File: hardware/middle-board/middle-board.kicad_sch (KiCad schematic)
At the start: 25 parts, among them J1 Conn_01x10_Socket, J2 Conn_01x15_Socket, J3 Conn_01x10_Pin, J4 Conn_01x09_Socket, J5 Conn_01x09_Socket, J6 Conn_01x12_Pin, U1 TL084, U2 TL074, U3 TL072, U4 NE5517

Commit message: wip - first pass done
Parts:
- C10, C3, C4, C5, C6, C7, C8, C9: footprint Capacitor_THT:C_Rect_L4.6mm_W3.0mm_P2.50mm_MKS02_FKP02 -> Eurorack Common:C_Disc_D3.4mm_W2.1mm_P2.50mm; symbol Device:C -> Eurorack Common:C_100nF_50V_X7R_2.5mm
- R1, R2, R3, R4, R5, R6, R7: footprint Resistor_THT:R_Axial_DIN0207_L6.3mm_D2.5mm_P7.62mm_Horizontal -> Eurorack Common:R_Axial_DIN0207_L6.3mm_D2.5mm_P7.62mm_Horizontal; symbol Device:R -> Eurorack Common:R_DIN0207
- U1: symbol Amplifier_Operational:TL084 -> Eurorack Common:TL084HIDYYR
- U2: footprint Package_DIP:DIP-14_W7.62mm -> Eurorack Common:DIP-14_W7.62mm; symbol Amplifier_Operational:TL074 -> Eurorack Common:TL074CN
- U3: footprint Package_DIP:DIP-8_W7.62mm -> Eurorack Common:DIP-8_W7.62mm; symbol Amplifier_Operational:TL072 -> Eurorack Common:TL072IP
- U4: footprint Package_SO:JEITA_SOIC-16_3.9x9.9mm_P1.27mm -> Eurorack Common:SOIC-16_3.9x9.9mm_P1.27mm; symbol Amplifier_Operational:LM13700 -> Eurorack Common:NE5517DR2G
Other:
- moved on the sheet: J1, J3

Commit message: chore: clean up the boards
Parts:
- J1: value Conn_01x10_Socket -> 01x10 Male Pin Header
- J2: value Conn_01x15_Socket -> 01x13 Female Pin Header
- J3: value Conn_01x10_Pin -> 01x10 Male Pin Header
- J4, J5: value Conn_01x09_Socket -> 01x09 Female Pin Header
- J6: value Conn_01x12_Pin -> 01x12 Female Pin Header
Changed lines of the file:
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@@
 			)
 		)
-		(property "Value" "Conn_01x10_Socket"
+		(property "Value" "01x10 Male Pin Header"
 			(at 66.294 88.9 0)
 			(effects
@@
 			)
 		)
-		(property "Value" "Conn_01x10_Pin"
+		(property "Value" "01x10 Male Pin Header"
 			(at 93.98 88.138 0)
 			(effects
@@
 			)
 		)
-		(property "Value" "Conn_01x12_Pin"
+		(property "Value" "01x12 Female Pin Header"
 			(at 102.87 36.068 0)
 			(effects
@@
 			)
 		)
-		(property "Value" "Conn_01x09_Socket"
+		(property "Value" "01x09 Female Pin Header"
 			(at 88.9 53.3399 0)
 			(effects
@@
 			)
 		)
-		(property "Value" "Conn_01x15_Socket"
+		(property "Value" "01x13 Female Pin Header"
 			(at 28.194 39.37 0)
 			(effects
@@
 			)
 		)
-		(property "Value" "Conn_01x09_Socket"
+		(property "Value" "01x09 Female Pin Header"
 			(at 51.562 37.338 0)
 			(effects

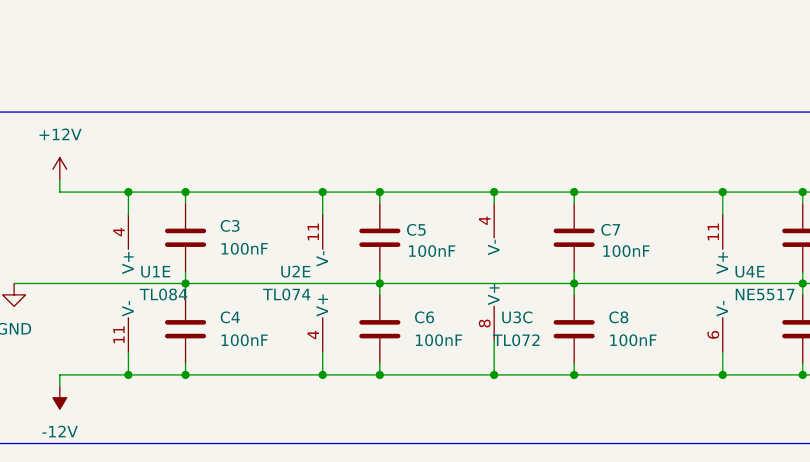
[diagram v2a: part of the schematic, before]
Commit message: fix: inverted power pins on op amps
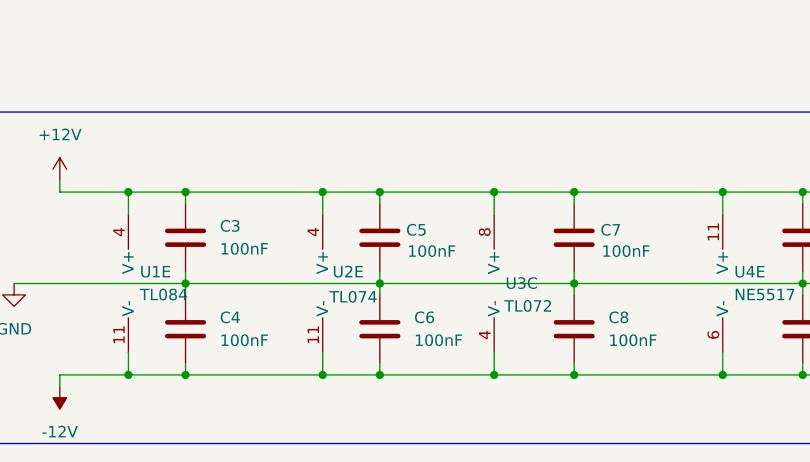
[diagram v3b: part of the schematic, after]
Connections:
- net +12V: now also U2.4 (V+), U3.8 (V+); no longer U2.11 (V-), U3.4 (V-)
- net -12V: now also U2.11 (V-), U3.4 (V-); no longer U2.4 (V+), U3.8 (V+)
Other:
- moved on the sheet: U3C
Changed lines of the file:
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@@
 	(wire
 		(pts
-			(xy 88.9 185.42) (xy 88.9 189.23)
+			(xy 88.9 186.69) (xy 88.9 189.23)
 		)
 		(stroke
@@
 	(wire
 		(pts
-			(xy 88.9 168.91) (xy 88.9 170.18)
+			(xy 88.9 168.91) (xy 88.9 171.45)
 		)
 		(stroke
@@
 	(symbol
 		(lib_id "Eurorack Common:TL072IP")
-		(at 91.44 177.8 0)
-		(mirror x)
+		(at 91.44 179.07 0)
 		(unit 3)
 		(exclude_from_sim no)
@@
 		(dnp no)
 		(property "Reference" "U3"
-			(at 91.44 182.88 0)
+			(at 91.948 179.07 0)
 			(effects
 				(font
@@
 		)
 		(property "Value" "TL072"
-			(at 91.44 185.42 0)
+			(at 92.71 181.61 0)
 			(effects
 				(font
@@
 		)
 		(property "Footprint" "Eurorack Common:DIP-8_W7.62mm"
-			(at 91.44 177.8 0)
+			(at 91.44 179.07 0)
 			(effects
 				(font
@@
 		)
 		(property "Datasheet" "http://www.ti.com/lit/ds/symlink/tl072.pdf"
-			(at 91.44 177.8 0)
+			(at 91.44 179.07 0)
 			(effects
 				(font
@@
 		)
 		(property "Description" "Dual Operational Amplifiers, DIP-8"
-			(at 91.44 177.8 0)
+			(at 91.44 179.07 0)
 			(effects
 				(font
@@
 		(lib_id "Eurorack Common:TL074CN")
 		(at 72.39 179.07 0)
-		(mirror x)
 		(unit 5)
 		(exclude_from_sim no)
@@
 		(on_board yes)
 		(dnp no)
-		(fields_autoplaced yes)
 		(property "Reference" "U2"
-			(at 68.58 177.7999 0)
+			(at 74.422 177.8 0)
 			(effects
 				(font
@@
 		)
 		(property "Value" "TL074"
-			(at 68.58 180.3399 0)
+			(at 75.946 180.594 0)
 			(effects
 				(font
@@
 		)
 		(property "Footprint" "Eurorack Common:DIP-14_W7.62mm"
-			(at 71.12 181.61 0)
+			(at 71.12 176.53 0)
 			(effects
 				(font
@@
 		)
 		(property "Datasheet" "http://www.ti.com/lit/ds/symlink/tl074.pdf"
-			(at 73.66 184.15 0)
+			(at 73.66 173.99 0)
 			(effects
 				(font
